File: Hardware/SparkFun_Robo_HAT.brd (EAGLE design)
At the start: 64.9 x 55.9 mm, 229 parts, among them J1 RASPBERRYPI-40-PIN-GPIO_PTH_R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, J11 EXT MTR PWR, J18 ISP, J20 USB C, J23 CORTEX_JTAG_DEBUG_PTH, J7 EXT SERVO PWR, J8 EXT 5V PWR, Q1 310mA/60V/1.6Ω, Q23 20V/0.2A/8MHz/1.2Ω/1Vth, Q24 20V/0.2A/8MHz/1.2Ω/1Vth, Q27 20V/0.2A/8MHz/1.2Ω/1Vth, Q28 20V/0.2A/8MHz/1.2Ω/1Vth, Q4 310mA/60V/1.6Ω, Q5 20V/4.2A/52mΩ/1.4W, Q7 20V/4.2A/52mΩ/1.4W, Q9 20V/4.2A/52mΩ/1.4W, U1 PCA9685, U4 ATTINY84-ARDUINO, U5 DRV8835, U6 CY8C4245LQI-483, U7 9DoF IMU, U8 1.8V/100mA

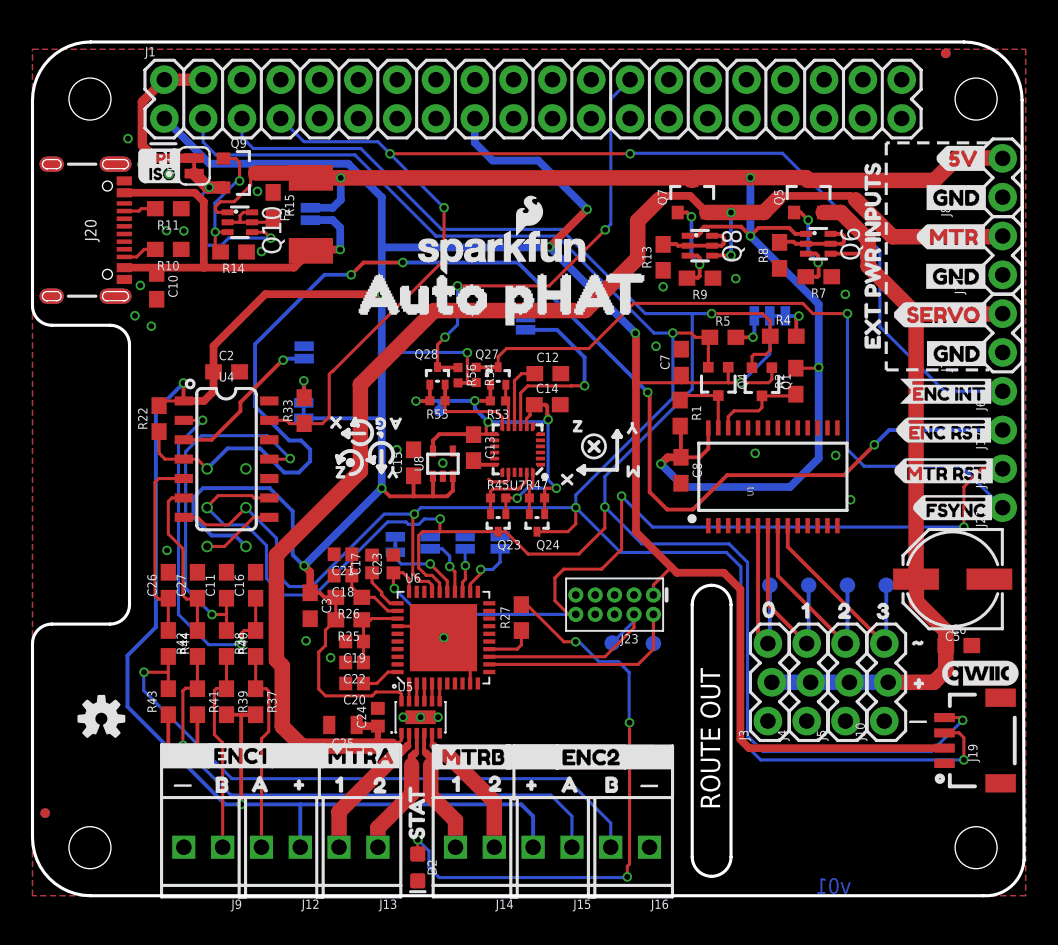
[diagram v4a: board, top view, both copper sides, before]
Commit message: Engineer 1st run of checklist
added measures and SS path, cleaned up sch a bit more.
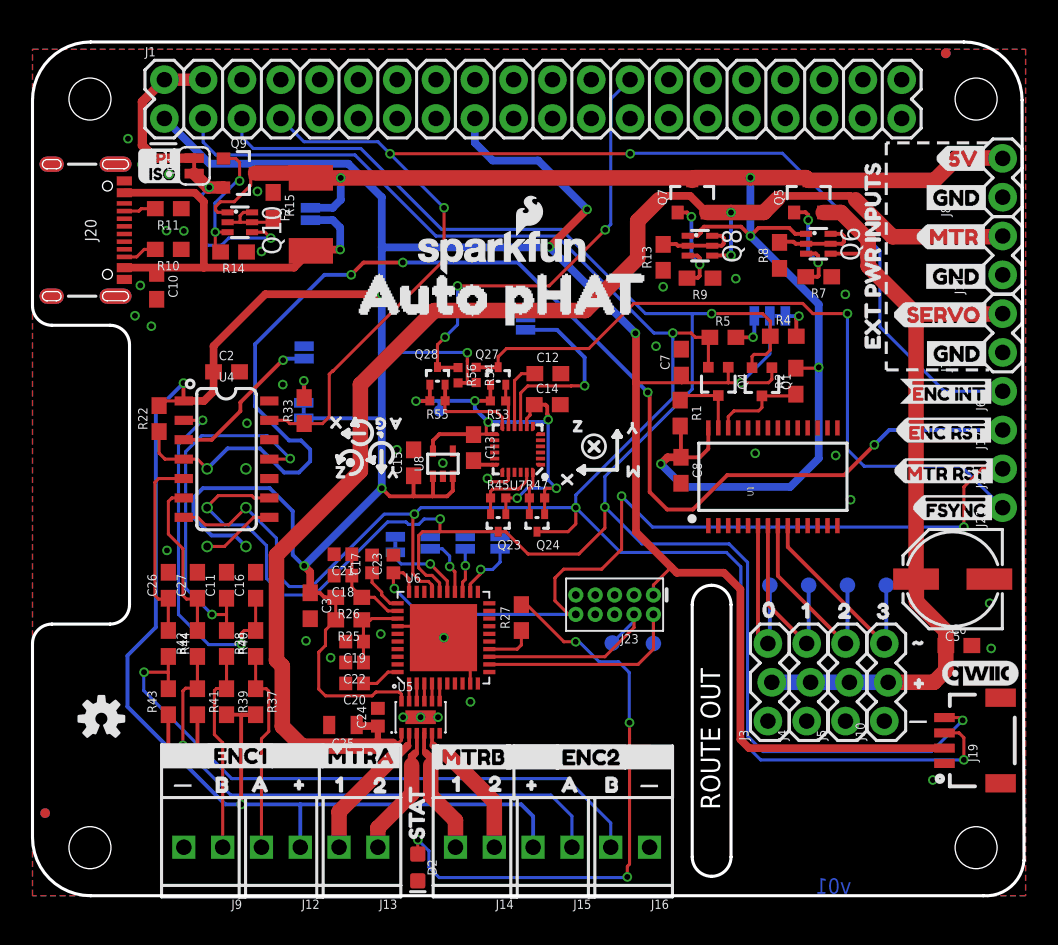
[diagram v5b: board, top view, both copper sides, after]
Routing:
- net GND: vias 26 -> 34
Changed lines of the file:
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@@
 <setting verticaltext="up"/>
 </settings>
-<grid distance="0.05" unitdist="inch" unit="inch" style="lines" multiple="1" display="yes" altdistance="0.0001" altunitdist="inch" altunit="inch"/>
+<grid distance="0.05" unitdist="inch" unit="inch" style="lines" multiple="1" display="yes" altdistance="0.001" altunitdist="inch" altunit="inch"/>
 <layers>
-<layer number="1" name="Top" color="4" fill="1" visible="no" active="yes"/>
+<layer number="1" name="Top" color="4" fill="1" visible="yes" active="yes"/>
 <layer number="15" name="Route15" color="4" fill="6" visible="no" active="no"/>
 <layer number="16" name="Bottom" color="1" fill="1" visible="yes" active="yes"/>
 <layer number="17" name="Pads" color="2" fill="1" visible="yes" active="yes"/>
 <layer number="18" name="Vias" color="2" fill="1" visible="yes" active="yes"/>
-<layer number="19" name="Unrouted" color="6" fill="1" visible="no" active="yes"/>
-<layer number="20" name="Dimension" color="24" fill="1" visible="no" active="yes"/>
-<layer number="21" name="tPlace" color="16" fill="1" visible="no" active="yes"/>
+<layer number="19" name="Unrouted" color="6" fill="1" visible="yes" active="yes"/>
+<layer number="20" name="Dimension" color="24" fill="1" visible="yes" active="yes"/>
+<layer number="21" name="tPlace" color="16" fill="1" visible="yes" active="yes"/>
 <layer number="22" name="bPlace" color="14" fill="1" visible="yes" active="yes"/>
-<layer number="23" name="tOrigins" color="15" fill="1" visible="no" active="yes"/>
+<layer number="23" name="tOrigins" color="15" fill="1" visible="yes" active="yes"/>
 <layer number="24" name="bOrigins" color="15" fill="1" visible="yes" active="yes"/>
 <layer number="25" name="tNames" color="7" fill="1" visible="no" active="yes"/>
@@
 <layer number="28" name="bValues" color="7" fill="1" visible="no" active="yes"/>
 <layer number="29" name="tStop" color="7" fill="3" visible="no" active="yes"/>
-<layer number="30" name="bStop" color="7" fill="6" visible="yes" active="yes"/>
+<layer number="30" name="bStop" color="7" fill="6" visible="no" active="yes"/>
 <layer number="31" name="tCream" color="7" fill="4" visible="no" active="yes"/>
 <layer number="32" name="bCream" color="7" fill="5" visible="no" active="yes"/>
@@
 <layer number="43" name="vRestrict" color="2" fill="10" visible="no" active="yes"/>
 <layer number="44" name="Drills" color="7" fill="1" visible="no" active="yes"/>
-<layer number="45" name="Holes" color="7" fill="1" visible="no" active="yes"/>
+<layer number="45" name="Holes" color="7" fill="1" visible="yes" active="yes"/>
 <layer number="46" name="Milling" color="3" fill="1" visible="no" active="yes"/>
 <layer number="47" name="Measures" color="7" fill="1" visible="no" active="yes"/>
 <layer number="48" name="Document" color="13" fill="7" visible="no" active="yes"/>
-<layer number="49" name="Reference" color="13" fill="1" visible="no" active="yes"/>
+<layer number="49" name="Reference" color="13" fill="1" visible="yes" active="yes"/>
 <layer number="50" name="dxf" color="7" fill="1" visible="no" active="yes"/>
-<layer number="51" name="tDocu" color="6" fill="1" visible="no" active="yes"/>
+<layer number="51" name="tDocu" color="6" fill="1" visible="yes" active="yes"/>
 <layer number="52" name="bDocu" color="7" fill="1" visible="no" active="yes"/>
 <layer number="91" name="Nets" color="2" fill="1" visible="no" active="no"/>
@@
 <vertex x="38.1" y="8.89"/>
 </polygon>
+<wire x1="9.0805" y1="3.23341875" x2="40.172640625" y2="3.23341875" width="6.6802" layer="48"/>
+<wire x1="40.172640625" y1="3.23341875" x2="40.421559375" y2="2.9845" width="6.6802" layer="48"/>
+<wire x1="46.3931" y1="16.04518125" x2="55.763159375" y2="16.04518125" width="6.6802" layer="48"/>
+<wire x1="55.763159375" y1="16.04518125" x2="55.844440625" y2="15.9639" width="6.6802" layer="48"/>
+<wire x1="55.844440625" y1="15.9639" x2="55.844440625" y2="10.617196875" width="6.6802" layer="48"/>
+<wire x1="55.844440625" y1="10.617196875" x2="55.88761875" y2="10.57401875" width="6.6802" layer="48"/>
+<wire x1="55.88761875" y1="10.57401875" x2="46.517559375" y2="10.57401875" width="6.6802" layer="48"/>
+<dimension x1="0" y1="52.07" x2="64.77" y2="50.8" x3="32.385" y3="64.77" textsize="1.778" layer="47" dtype="horizontal" unit="inch" visible="yes"/>
+<dimension x1="62.23" y1="0" x2="59.69" y2="55.88" x3="74.93" y3="27.94" textsize="1.778" layer="47" dtype="vertical" unit="inch" visible="yes"/>
+<dimension x1="3.81" y1="0" x2="3.81" y2="3.175" x3="-5.334" y3="1.5875" textsize="1.778" layer="47" dtype="vertical" unit="inch" visible="yes"/>
+<dimension x1="0" y1="52.07" x2="61.722" y2="52.07" x3="30.861" y3="72.39" textsize="1.778" layer="47" dtype="horizontal" unit="inch" visible="yes"/>
+<dimension x1="62.23" y1="0" x2="61.722" y2="3.175" x3="82.55" y3="1.5875" textsize="1.778" layer="47" dtype="vertical" unit="inch" visible="yes"/>
+<dimension x1="60.96" y1="55.88" x2="60.96" y2="51.943" x3="80.645" y3="53.9115" textsize="1.778" layer="47" dtype="vertical" unit="inch" visible="yes"/>
+<dimension x1="3.81" y1="55.88" x2="3.937" y2="51.943" x3="-15.113" y3="53.9115" textsize="1.778" layer="47" dtype="vertical" unit="inch" visible="yes"/>
+<dimension x1="3.81" y1="0" x2="3.81" y2="51.943" x3="-20.32" y3="25.9715" textsize="1.778" layer="47" dtype="vertical" unit="inch" visible="yes"/>
+<dimension x1="0" y1="3.81" x2="8.4582" y2="0.381" x3="4.2291" y3="-5.6134" textsize="1.778" layer="47" dtype="horizontal" unit="inch" visible="yes"/>
+<dimension x1="0" y1="3.81" x2="24.1046" y2="0.254" x3="12.0523" y3="-10.5918" textsize="1.778" layer="47" dtype="horizontal" unit="inch" visible="yes"/>
+<dimension x1="0" y1="3.81" x2="26.2128" y2="1.4732" x3="13.1064" y3="-17.5006" textsize="1.778" layer="47" dtype="horizontal" unit="inch" visible="yes"/>
+<dimension x1="0" y1="3.81" x2="41.8846" y2="1.2954" x3="20.9423" y3="-23.7998" textsize="1.778" layer="47" dtype="horizontal" unit="inch" visible="yes"/>
+<dimension x1="0" y1="3.81" x2="48.133" y2="11.4554" x3="24.0665" y3="-29.7688" textsize="1.778" layer="47" dtype="horizontal" unit="inch" visible="yes"/>
+<dimension x1="0" y1="3.81" x2="55.753" y2="11.4554" x3="27.8765" y3="-35.2806" textsize="1.778" layer="47" dtype="horizontal" unit="inch" visible="yes"/>
+<dimension x1="3.81" y1="55.88" x2="6.35" y2="43.561" x3="-27.7622" y3="49.7205" textsize="1.778" layer="47" dtype="vertical" unit="inch" visible="yes"/>
+<dimension x1="62.23" y1="0" x2="59.69" y2="10.16" x3="92.3798" y3="5.08" textsize="1.778" layer="47" dtype="vertical" unit="inch" visible="yes"/>
 </plain>
 <attributes>
@@
 <contactref element="J23" pad="7"/>
 <contactref element="J23" pad="9"/>
+<via x="22.791421875" y="17.129759375" extent="1-16" drill="0.381"/>
+<via x="28.66644375" y="12.69238125" extent="1-16" drill="0.381"/>
+<via x="16.383003125" y="33.456884375" extent="1-16" drill="0.381"/>
+<via x="14.03604375" y="30.924503125" extent="1-16" drill="0.381"/>
+<via x="29.776421875" y="27.310084375" extent="1-16" drill="0.381"/>
+<via x="62.646565625" y="19.146521875" extent="1-16" drill="0.381"/>
+<via x="62.745625" y="16.187421875" extent="1-16" drill="0.381"/>
+<via x="58.928003125" y="7.57428125" extent="1-16" drill="0.381"/>
 </signal>
 <signal name="SCL_3.3V">
@@
 <contactref element="Q6" pad="3"/>
 <contactref element="R7" pad="2"/>
-<wire x1="49.85" y1="44.72" x2="50.276" y2="44.72" width="0.254" layer="1"/>
-<wire x1="50.276" y1="44.72" x2="50.772059375" y2="44.223940625" width="0.254" layer="1"/>
+<wire x1="50.590959375" y1="44.7352375" x2="49.8652375" y2="44.7352375" width="0.254" layer="1"/>
+<wire x1="49.85" y1="44.72" x2="49.8652375" y2="44.7352375" width="0.254" layer="1"/>
+<wire x1="50.772059375" y1="44.5541375" x2="50.772059375" y2="44.223940625" width="0.254" layer="1"/>
+<wire x1="50.772059375" y1="44.5541375" x2="50.590959375" y2="44.7352375" width="0.254" layer="1"/>
 <via x="50.772059375" y="44.223940625" extent="1-16" drill="0.381"/>
 <wire x1="50.772059375" y1="44.223940625" x2="50.772059375" y2="42.09164375" width="0.254" layer="16"/>

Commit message: post design review changes
-moved TP P3.0 programming pSoc onto grid
-Added pulldown resistor on Config line on PSoc
-Added trestric under pSoC to avoid GND pad nubbins.
-Added pullup resistors to SDA_OUT and SCL_OUT, as consistent with original serial controlled motor driver.
-Switched over to design block for pi header and slots. re-routed some stuff to make it work.
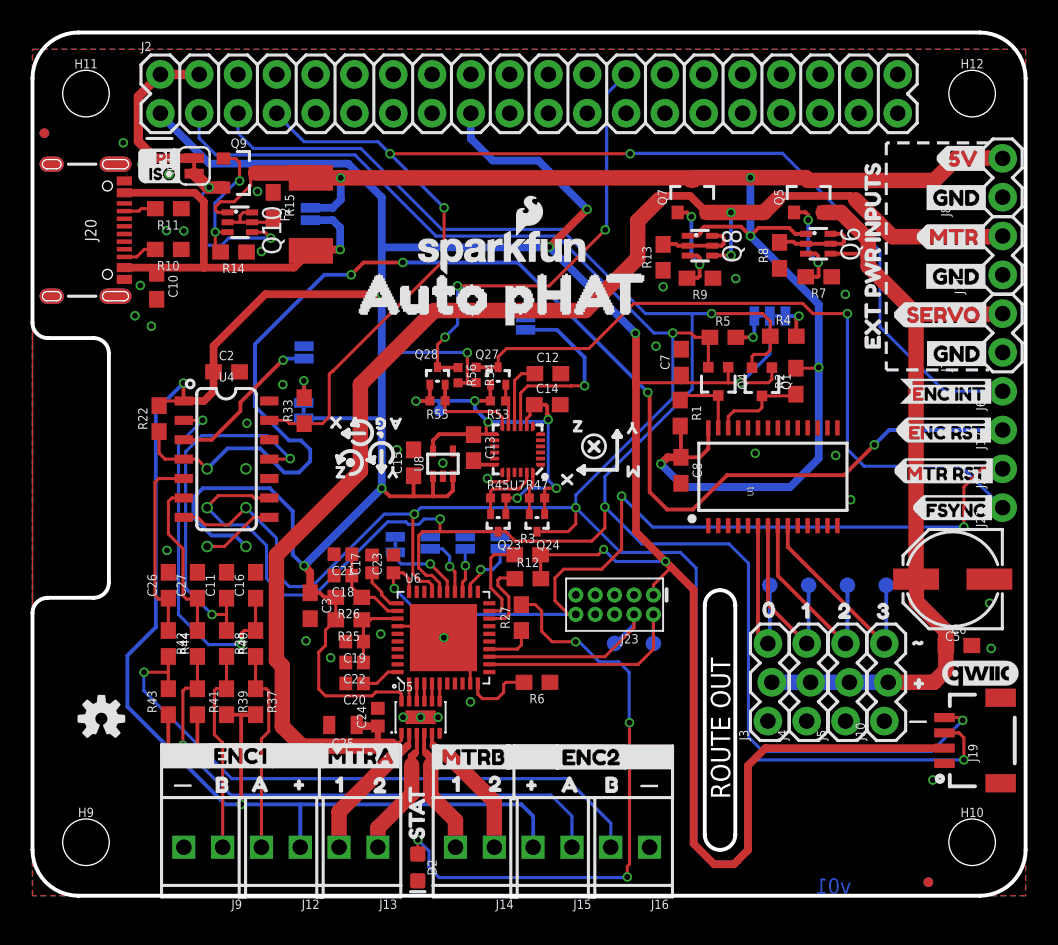
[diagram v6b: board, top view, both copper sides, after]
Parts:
- removed FD1, FD2, FD3, FD4: FIDUCIALUFIDUCIAL, SparkFun-Aesthetics:FIDUCIAL-MICRO
- removed J1: RASPBERRYPI-40-PIN-GPIO_PTH_REFERENCE, SparkFun-Connectors:RASPBERRY_PI_HAT_40_PIN_PTH_WITH_REFERNCE
- added FD5, FD6, FD7, FD8: FIDUCIALUFIDUCIAL, SparkFun-Aesthetics:FIDUCIAL-MICRO
- added H10, H11, H12, H9: STAND-OFFTIGHT, SparkFun-Hardware:STAND-OFF-TIGHT
- added J2: RASPBERRYPI-40-PIN-GPIO_PTH_NO_SHROUD, SparkFun-Connectors:2X20
- added R12, R3, R6: 5.1k, SparkFun-Resistors:0603@1
- R1, R10, R11, R13, R14, R15, R2, R22, R25, R26, R27, R33, R37, R38, R39, R4, R40, R41, R42, R43, R44, R5, R7, R8, R9: device SparkFun-Resistors:0603 -> SparkFun-Resistors:0603@1
- moved TP8 0.16 mm to (38.1, 16.5)
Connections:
- new net CONFIG_OUT: R6.2, U6.10
- new net SCL_OUT: R12.1, U6.18
- new net SDA_OUT: R3.1, U6.19
- net !ENC_INT: now also J2.7; no longer J1.7
- net 3.3V: now also J2.1, J2.17, R12.2, R3.2; no longer J1.1, J1.17
- net GND: now also J2.14, J2.20, J2.25, J2.30, J2.34, J2.39, J2.6, J2.9, R6.1; no longer J1.14, J1.20, J1.25, J1.30, J1.34, J1.39, J1.6, J1.9
- net IMU_INT_3.3V: now also J2.26; no longer J1.26
- net N$20: now also J2.2, J2.4; no longer J1.2, J1.4
- net SCL_3.3V: now also J2.5; no longer J1.5
- net SDA_3.3V: now also J2.3; no longer J1.3
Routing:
- net 3.3V: track 289.1 -> 313.7 mm, vias 11 -> 13
- net SDA_3.3V: track 139.5 -> 152.6 mm
- net SDA_OUT: track 0.00 -> 6.17 mm
- net SCL_OUT: track 0.00 -> 5.30 mm
- net CONFIG_OUT: track 0.00 -> 4.58 mm
- net N$27: track 38.7 -> 39.4 mm
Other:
- board size 64.9 x 55.9 mm -> 65 x 56.5 mm
